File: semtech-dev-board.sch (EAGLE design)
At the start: 58 parts, among them Q1 BSS123, U1 MIC5219 3.3V, U2 QUALCOMM-TDK_B3710, U3 QUALCOMM-TDK_B3588, U4 SEMTECH_SX1236, Y1 32MHz

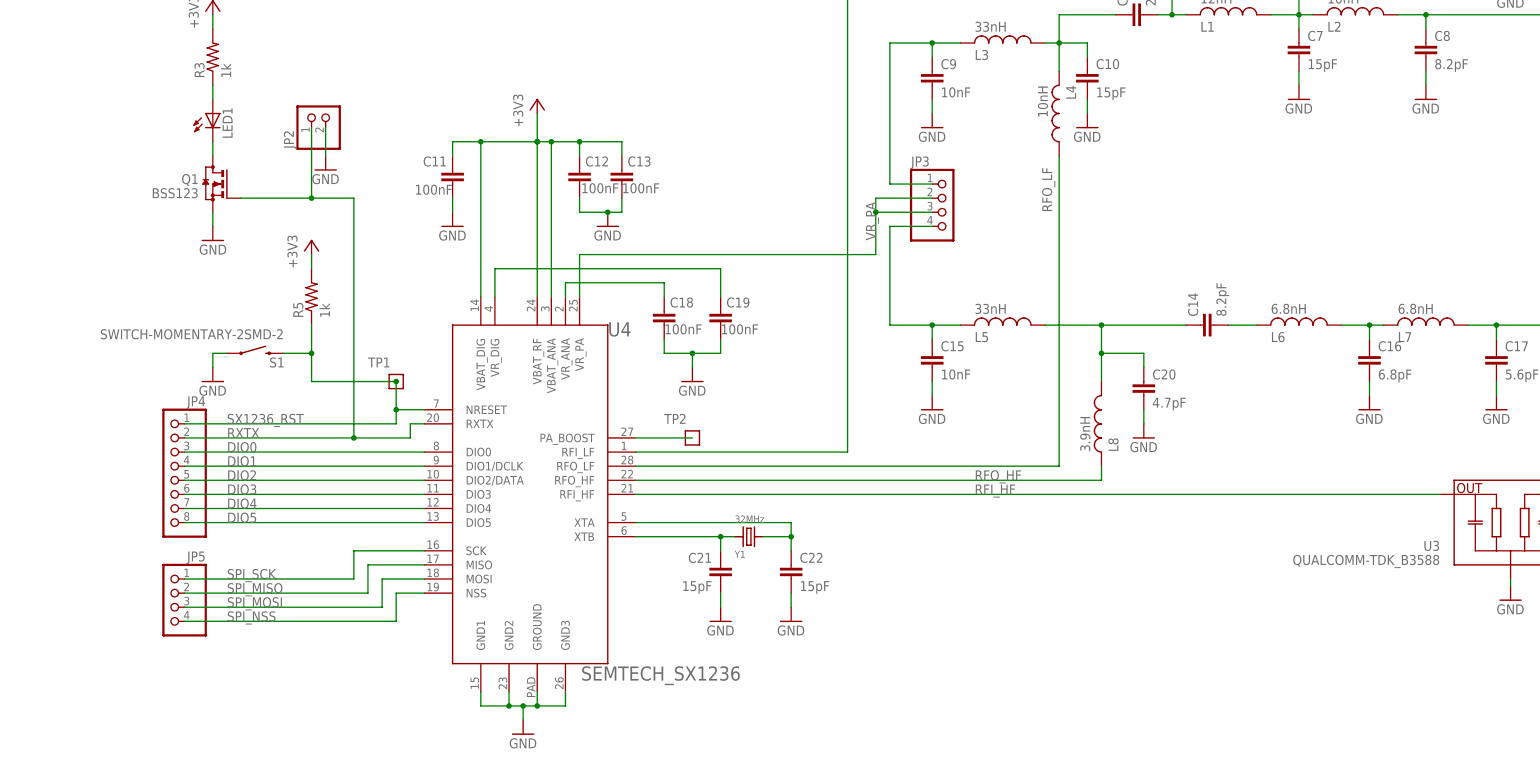
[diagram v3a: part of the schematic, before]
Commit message: TNAMES cleanup, better ground plane splitting - probably TOTALLY unnecessary on this board, but whatevs, it's fun. Updated SX1236 symbol, switched digital/analog caps to be correct.
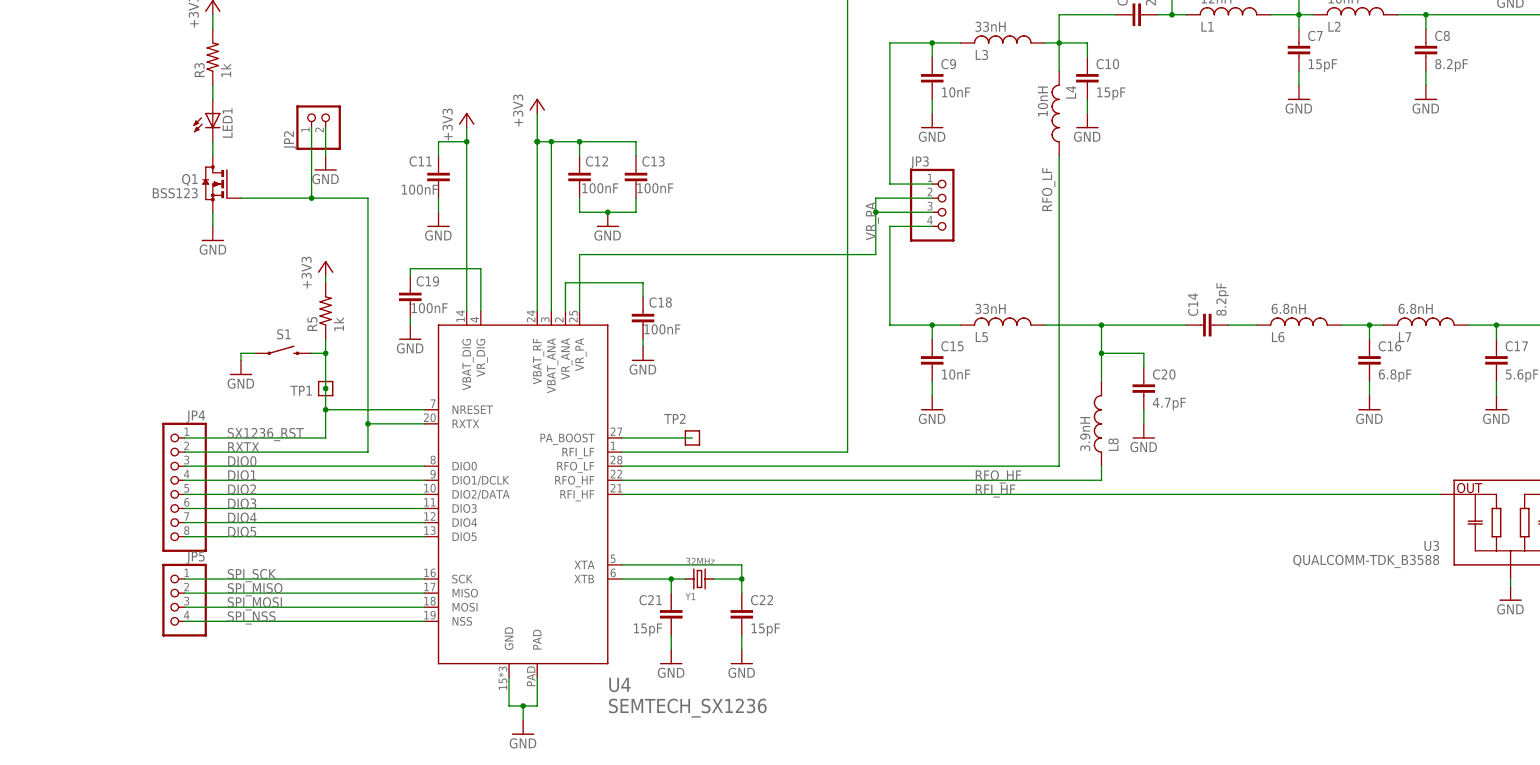
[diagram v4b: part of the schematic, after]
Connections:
- net GND: now also U4.GND, U4.PAD; no longer U4.GND1, U4.GND2, U4.GND3, U4.GROUND
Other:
- moved on the sheet: C11, C13, C18, C19, C21, C22, JP4, R5, S1, TP1, Y1

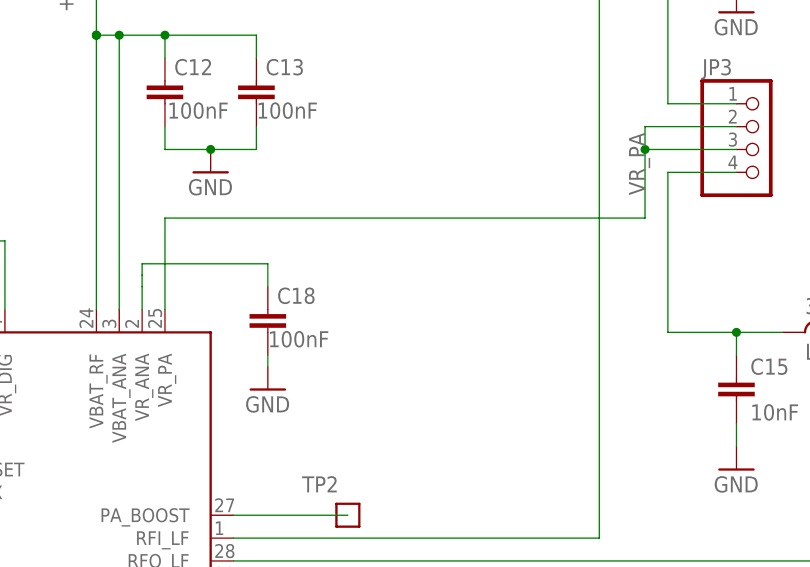
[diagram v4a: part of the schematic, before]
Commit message: Added cap to VR_PA, because it said to. Probably overkill, given the other ones.
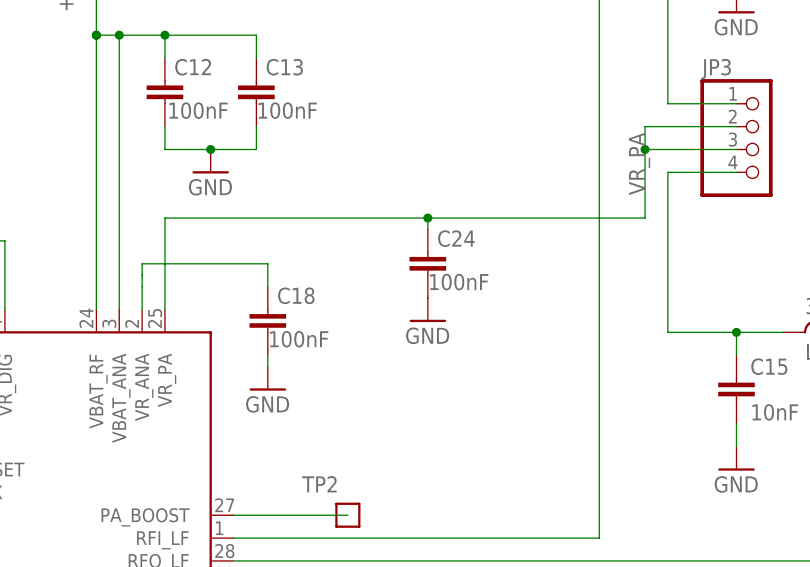
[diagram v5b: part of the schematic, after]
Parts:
- added C24: 100nF, rcl_custom:C-EU0603-B-NOSILK
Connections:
- net GND: now also C24.2
- net VR_PA: now also C24.1
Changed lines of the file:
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@@
 <setting verticaltext="up"/>
 </settings>
-<grid distance="0.1" unitdist="inch" unit="inch" style="lines" multiple="1" display="no" altdistance="0.01" altunitdist="inch" altunit="inch"/>
+<grid distance="0.05" unitdist="inch" unit="inch" style="lines" multiple="1" display="no" altdistance="0.01" altunitdist="inch" altunit="inch"/>
 <layers>
 <layer number="1" name="Top" color="4" fill="1" visible="no" active="no"/>
@@
 <part name="GND30" library="supply1" deviceset="GND" device=""/>
 <part name="U4" library="low-gain-radio" deviceset="SEMTECH_SX1236" device=""/>
+<part name="C24" library="rcl_custom" deviceset="C-EU" device="0603-B-NOSILK" value="100nF"/>
+<part name="GND31" library="supply1" deviceset="GND" device=""/>
 </parts>
 <sheets>
@@
 <attribute name="VALUE" x="147.32" y="41.91" size="2.54" layer="96"/>
 </instance>
+<instance part="C24" gate="CE" x="171.45" y="120.65" smashed="yes">
+<attribute name="NAME" x="172.466" y="121.285" size="1.778" layer="95"/>
+<attribute name="VALUE" x="171.45" y="116.459" size="1.778" layer="96"/>
+</instance>
+<instance part="GND31" gate="1" x="171.45" y="113.03"/>
 </instances>
 <busses>
@@
 <pinref part="GND24" gate="1" pin="GND"/>
 <wire x1="342.9" y1="73.66" x2="342.9" y2="74.93" width="0.1524" layer="91"/>
+</segment>
+<segment>
+<pinref part="C24" gate="CE" pin="2"/>
+<pinref part="GND31" gate="1" pin="GND"/>
 </segment>
 </net>
@@
 <wire x1="195.58" y1="134.62" x2="195.58" y2="132.08" width="0.1524" layer="91"/>
 <wire x1="195.58" y1="132.08" x2="195.58" y2="124.46" width="0.1524" layer="91"/>
-<wire x1="142.24" y1="124.46" x2="195.58" y2="124.46" width="0.1524" layer="91"/>
 <label x="195.58" y="127" size="1.778" layer="95" rot="R90"/>
 <pinref part="JP3" gate="A" pin="2"/>
@@
 <junction x="195.58" y="132.08"/>
 <pinref part="U4" gate="G$1" pin="VR_PA"/>
-</segment>
-</net>
+<pinref part="C24" gate="CE" pin="1"/>
+<wire x1="142.24" y1="124.46" x2="171.45" y2="124.46" width="0.1524" layer="91"/>
+<wire x1="171.45" y1="124.46" x2="195.58" y2="124.46" width="0.1524" layer="91"/>
+<wire x1="171.45" y1="123.19" x2="171.45" y2="124.46" width="0.1524" layer="91"/>
+<junction x="171.45" y="124.46"/>
+</segment>
+</net>

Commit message: Added updated BOM, and adjusted inductor sizes
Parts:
- L4, L5: device rcl:L-USL3225P -> rcl:L-USL3225M
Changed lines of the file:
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@@
 <setting verticaltext="up"/>
 </settings>
-<grid distance="0.05" unitdist="inch" unit="inch" style="lines" multiple="1" display="no" altdistance="0.01" altunitdist="inch" altunit="inch"/>
+<grid distance="0.1" unitdist="inch" unit="inch" style="lines" multiple="1" display="no" altdistance="0.01" altunitdist="inch" altunit="inch"/>
 <layers>
-<layer number="1" name="Top" color="4" fill="1" visible="no" active="no"/>
-<layer number="2" name="Route2" color="1" fill="3" visible="no" active="no"/>
-<layer number="3" name="Route3" color="4" fill="3" visible="no" active="no"/>
-<layer number="4" name="Route4" color="1" fill="4" visible="no" active="no"/>
-<layer number="5" name="Route5" color="4" fill="4" visible="no" active="no"/>
-<layer number="6" name="Route6" color="1" fill="8" visible="no" active="no"/>
-<layer number="7" name="Route7" color="4" fill="8" visible="no" active="no"/>
-<layer number="8" name="Route8" color="1" fill="2" visible="no" active="no"/>
-<layer number="9" name="Route9" color="4" fill="2" visible="no" active="no"/>
-<layer number="10" name="Route10" color="1" fill="7" visible="no" active="no"/>
-<layer number="11" name="Route11" color="4" fill="7" visible="no" active="no"/>
-<layer number="12" name="Route12" color="1" fill="5" visible="no" active="no"/>
-<layer number="13" name="Route13" color="4" fill="5" visible="no" active="no"/>
-<layer number="14" name="Route14" color="1" fill="6" visible="no" active="no"/>
-<layer number="15" name="Route15" color="4" fill="6" visible="no" active="no"/>
-<layer number="16" name="Bottom" color="1" fill="1" visible="no" active="no"/>
-<layer number="17" name="Pads" color="2" fill="1" visible="no" active="no"/>
-<layer number="18" name="Vias" color="2" fill="1" visible="no" active="no"/>
-<layer number="19" name="Unrouted" color="6" fill="1" visible="no" active="no"/>
-<layer number="20" name="Dimension" color="15" fill="1" visible="no" active="no"/>
-<layer number="21" name="tPlace" color="7" fill="1" visible="no" active="no"/>
-<layer number="22" name="bPlace" color="7" fill="1" visible="no" active="no"/>
-<layer number="23" name="tOrigins" color="15" fill="1" visible="no" active="no"/>
-<layer number="24" name="bOrigins" color="15" fill="1" visible="no" active="no"/>
-<layer number="25" name="tNames" color="7" fill="1" visible="no" active="no"/>
-<layer number="26" name="bNames" color="7" fill="1" visible="no" active="no"/>
-<layer number="27" name="tValues" color="7" fill="1" visible="no" active="no"/>
-<layer number="28" name="bValues" color="7" fill="1" visible="no" active="no"/>
+<layer number="1" name="Top" color="4" fill="1" visible="yes" active="no"/>
+<layer number="2" name="Route2" color="15" fill="1" visible="yes" active="no"/>
+<layer number="3" name="Route3" color="4" fill="3" visible="yes" active="no"/>
+<layer number="4" name="Route4" color="1" fill="4" visible="yes" active="no"/>
+<layer number="5" name="Route5" color="4" fill="4" visible="yes" active="no"/>
+<layer number="6" name="Route6" color="1" fill="8" visible="yes" active="no"/>
+<layer number="7" name="Route7" color="4" fill="8" visible="yes" active="no"/>
+<layer number="8" name="Route8" color="1" fill="2" visible="yes" active="no"/>
+<layer number="9" name="Route9" color="4" fill="2" visible="yes" active="no"/>
+<layer number="10" name="Route10" color="1" fill="7" visible="yes" active="no"/>
+<layer number="11" name="Route11" color="4" fill="7" visible="yes" active="no"/>
+<layer number="12" name="Route12" color="1" fill="5" visible="yes" active="no"/>
+<layer number="13" name="Route13" color="4" fill="5" visible="yes" active="no"/>
+<layer number="14" name="Route14" color="1" fill="6" visible="yes" active="no"/>
+<layer number="15" name="Route15" color="14" fill="1" visible="yes" active="no"/>
+<layer number="16" name="Bottom" color="1" fill="1" visible="yes" active="no"/>
+<layer number="17" name="Pads" color="2" fill="1" visible="yes" active="no"/>
+<layer number="18" name="Vias" color="2" fill="1" visible="yes" active="no"/>
+<layer number="19" name="Unrouted" color="6" fill="1" visible="yes" active="no"/>
+<layer number="20" name="Dimension" color="15" fill="1" visible="yes" active="no"/>
+<layer number="21" name="tPlace" color="7" fill="1" visible="yes" active="no"/>
+<layer number="22" name="bPlace" color="7" fill="1" visible="yes" active="no"/>
+<layer number="23" name="tOrigins" color="15" fill="1" visible="yes" active="no"/>
+<layer number="24" name="bOrigins" color="15" fill="1" visible="yes" active="no"/>
+<layer number="25" name="tNames" color="7" fill="1" visible="yes" active="no"/>
+<layer number="26" name="bNames" color="7" fill="1" visible="yes" active="no"/>
+<layer number="27" name="tValues" color="7" fill="1" visible="yes" active="no"/>
+<layer number="28" name="bValues" color="7" fill="1" visible="yes" active="no"/>
 <layer number="29" name="tStop" color="7" fill="3" visible="no" active="no"/>
 <layer number="30" name="bStop" color="7" fill="6" visible="no" active="no"/>
@@
 <layer number="35" name="tGlue" color="7" fill="4" visible="no" active="no"/>
 <layer number="36" name="bGlue" color="7" fill="5" visible="no" active="no"/>
-<layer number="37" name="tTest" color="7" fill="1" visible="no" active="no"/>
-<layer number="38" name="bTest" color="7" fill="1" visible="no" active="no"/>
+<layer number="37" name="tTest" color="7" fill="1" visible="yes" active="no"/>
+<layer number="38" name="bTest" color="7" fill="1" visible="yes" active="no"/>
 <layer number="39" name="tKeepout" color="4" fill="11" visible="no" active="no"/>
 <layer number="40" name="bKeepout" color="1" fill="11" visible="no" active="no"/>
@@
 <layer number="44" name="Drills" color="7" fill="1" visible="no" active="no"/>
 <layer number="45" name="Holes" color="7" fill="1" visible="no" active="no"/>
-<layer number="46" name="Milling" color="3" fill="1" visible="no" active="no"/>
-<layer number="47" name="Measures" color="7" fill="1" visible="no" active="no"/>
-<layer number="48" name="Document" color="7" fill="1" visible="no" active="no"/>
-<layer number="49" name="Reference" color="7" fill="1" visible="no" active="no"/>
-<layer number="50" name="dxf" color="7" fill="1" visible="no" active="no"/>
-<layer number="51" name="tDocu" color="7" fill="1" visible="no" active="no"/>
-<layer number="52" name="bDocu" color="7" fill="1" visible="no" active="no"/>
-<layer number="53" name="tGND_GNDA" color="7" fill="1" visible="no" active="no"/>
-<layer number="54" name="bGND_GNDA" color="7" fill="1" visible="no" active="no"/>
-<layer number="56" name="wert" color="7" fill="1" visible="no" active="no"/>
-<layer number="57" name="tCAD" color="7" fill="1" visible="no" active="no"/>
-<layer number="58" name="b3D" color="7" fill="1" visible="no" active="no"/>
-<layer number="59" name="Invisible" color="7" fill="1" visible="no" active="no"/>
-<layer number="60" name="bCarbon" color="7" fill="1" visible="no" active="no"/>
-<layer number="61" name="stand" color="7" fill="1" visible="no" active="no"/>
+<layer number="46" name="Milling" color="3" fill="1" visible="yes" active="no"/>
+<layer number="47" name="Measures" color="7" fill="1" visible="yes" active="no"/>
+<layer number="48" name="Document" color="7" fill="1" visible="yes" active="no"/>
+<layer number="49" name="Reference" color="7" fill="1" visible="yes" active="no"/>
+<layer number="50" name="dxf" color="7" fill="1" visible="yes" active="no"/>
+<layer number="51" name="tDocu" color="7" fill="1" visible="yes" active="no"/>
+<layer number="52" name="bDocu" color="7" fill="1" visible="yes" active="no"/>
+<layer number="53" name="tGND_GNDA" color="7" fill="1" visible="yes" active="no"/>
+<layer number="54" name="bGND_GNDA" color="7" fill="1" visible="yes" active="no"/>
+<layer number="56" name="wert" color="7" fill="1" visible="yes" active="no"/>
+<layer number="57" name="tCAD" color="7" fill="1" visible="yes" active="no"/>
+<layer number="58" name="b3D" color="7" fill="1" visible="yes" active="no"/>
+<layer number="59" name="Invisible" color="7" fill="1" visible="yes" active="no"/>
+<layer number="60" name="bCarbon" color="7" fill="1" visible="yes" active="no"/>
+<layer number="61" name="stand" color="7" fill="1" visible="yes" active="no"/>
 <layer number="90" name="Modules" color="5" fill="1" visible="yes" active="yes"/>
 <layer number="91" name="Nets" color="2" fill="1" visible="yes" active="yes"/>
@@
 <part name="GND15" library="supply1" deviceset="GND" device=""/>
 <part name="C9" library="rcl_custom" deviceset="C-EU" device="0603-B-NOSILK" value="10nF"/>
-<part name="L4" library="rcl" library_urn="urn:adsk.eagle:library:334" deviceset="L-US" device="L3225P" value="10nH"/>
+<part name="L4" library="rcl" library_urn="urn:adsk.eagle:library:334" deviceset="L-US" device="L3225M" value="10nH"/>
 <part name="L3" library="rcl" library_urn="urn:adsk.eagle:library:334" deviceset="L-US" device="L3225M" value="33nH"/>
 <part name="C10" library="rcl_custom" deviceset="C-EU" device="0603-B-NOSILK" value="15pF"/>
@@
 <part name="C17" library="rcl_custom" deviceset="C-EU" device="0603-B-NOSILK" value="5.6pF"/>
 <part name="L8" library="rcl" library_urn="urn:adsk.eagle:library:334" deviceset="L-US" device="L3225M" value="3.9nH"/>
-<part name="L5" library="rcl" library_urn="urn:adsk.eagle:library:334" deviceset="L-US" device="L3225P" value="33nH"/>
+<part name="L5" library="rcl" library_urn="urn:adsk.eagle:library:334" deviceset="L-US" device="L3225M" value="33nH"/>
 <part name="C15" library="rcl_custom" deviceset="C-EU" device="0603-B-NOSILK" value="10nF"/>
 <part name="JP3" library="pinhead" library_urn="urn:adsk.eagle:library:325" deviceset="PINHD-1X4" device=""/>
